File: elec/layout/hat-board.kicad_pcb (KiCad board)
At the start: 2 copper layers, 108 x 115.9 mm, 26 parts, among them U1 _NXP_Semicon_PN5321A3HN_C106_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

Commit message: 50% layout for hat
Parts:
- added C17: , lcsc:C0402, F.Cu at (104.4, 112.2)
- added C18: , lcsc:C0402, F.Cu at (109.7, 123.4)
- added C19: , lcsc:C0402, F.Cu at (179.3, 44.5)
- added C20: , lcsc:C0402, F.Cu at (188.8, 52.5)
- added C21: , lcsc:C0402, F.Cu at (196.0, 62.8)
- added C22: , lcsc:C0402, F.Cu at (164.1, 144.6)
- added C23: , lcsc:C0402, F.Cu at (139.4, 144.8)
- added C24: , lcsc:C0402, F.Cu at (117.7, 133.0)
- added C25: , lcsc:C0402, F.Cu at (101.9, 100.0)
- added C26: , lcsc:C0402, F.Cu at (101.8, 86.9)
- added C27: , lcsc:C0402, F.Cu at (201.9, 86.8)
- added C28: 100nF ±10% 16V X7R, lcsc:C0402, F.Cu at (201.8, 99.9)
- added C29: , lcsc:C0402, F.Cu at (200.4, 74.4)
- added C30: , lcsc:C0402, F.Cu at (173.9, 140.9)
- added C31: , lcsc:C0402, F.Cu at (129.5, 140.9)
- added C32: , lcsc:C0402, F.Cu at (151.7, 146.2)
- added C33: , lcsc:C0402, F.Cu at (107.6, 62.8)
- added C34: , lcsc:C0402, F.Cu at (103.2, 74.5)
- added C35: , lcsc:C0402, F.Cu at (193.8, 123.4)
- added C36: , lcsc:C0402, F.Cu at (185.8, 133.0)
- added C37: , lcsc:C0402, F.Cu at (199.3, 112.3)
- added C38: , lcsc:C0402, F.Cu at (114.8, 52.5)
- added C39: , lcsc:C0402, F.Cu at (124.3, 44.6)
- added U10: _OPSCO_Optoelectronics_SK6805SIDE_G_001, lcsc:LED-SMD_4P-L3.5-W1.6_SK6805SIDE-G-001, F.Cu at (100.6, 100.0)
- added U11: _OPSCO_Optoelectronics_SK6805SIDE_G_001, lcsc:LED-SMD_4P-L3.5-W1.6_SK6805SIDE-G-001, F.Cu at (100.4, 86.8)
- added U12: _OPSCO_Optoelectronics_SK6805SIDE_G_001, lcsc:LED-SMD_4P-L3.5-W1.6_SK6805SIDE-G-001, F.Cu at (101.9, 74.1)
- added U13: _OPSCO_Optoelectronics_SK6805SIDE_G_001, lcsc:LED-SMD_4P-L3.5-W1.6_SK6805SIDE-G-001, F.Cu at (189.8, 51.7)
- added U14: _OPSCO_Optoelectronics_SK6805SIDE_G_001, lcsc:LED-SMD_4P-L3.5-W1.6_SK6805SIDE-G-001, F.Cu at (106.4, 62.1)
- added U15: _OPSCO_Optoelectronics_SK6805SIDE_G_001, lcsc:LED-SMD_4P-L3.5-W1.6_SK6805SIDE-G-001, F.Cu at (113.8, 51.7)
- added U16: _OPSCO_Optoelectronics_SK6805SIDE_G_001, lcsc:LED-SMD_4P-L3.5-W1.6_SK6805SIDE-G-001, F.Cu at (123.5, 43.4)
- added U17: _OPSCO_Optoelectronics_SK6805SIDE_G_001, lcsc:LED-SMD_4P-L3.5-W1.6_SK6805SIDE-G-001, F.Cu at (197.2, 62.1)
- added U18: _OPSCO_Optoelectronics_SK6805SIDE_G_001, lcsc:LED-SMD_4P-L3.5-W1.6_SK6805SIDE-G-001, F.Cu at (201.7, 74.0)
- added U19: _OPSCO_Optoelectronics_SK6805SIDE_G_001, lcsc:LED-SMD_4P-L3.5-W1.6_SK6805SIDE-G-001, F.Cu at (203.2, 86.8)
- added U2: _OPSCO_Optoelectronics_SK6805SIDE_G_001, lcsc:LED-SMD_4P-L3.5-W1.6_SK6805SIDE-G-001, F.Cu at (180.1, 43.4)
- added U20: _OPSCO_Optoelectronics_SK6805SIDE_G_001, lcsc:LED-SMD_4P-L3.5-W1.6_SK6805SIDE-G-001, F.Cu at (203.0, 100.0)
- added U21: _OPSCO_Optoelectronics_SK6805SIDE_G_001, lcsc:LED-SMD_4P-L3.5-W1.6_SK6805SIDE-G-001, F.Cu at (200.5, 112.6)
- added U22: _OPSCO_Optoelectronics_SK6805SIDE_G_001, lcsc:LED-SMD_4P-L3.5-W1.6_SK6805SIDE-G-001, F.Cu at (195.0, 124.1)
- added U23: _OPSCO_Optoelectronics_SK6805SIDE_G_001, lcsc:LED-SMD_4P-L3.5-W1.6_SK6805SIDE-G-001, F.Cu at (186.7, 133.8)
- added U24: _OPSCO_Optoelectronics_SK6805SIDE_G_001, lcsc:LED-SMD_4P-L3.5-W1.6_SK6805SIDE-G-001, F.Cu at (176.4, 141.3)
- added U3: _OPSCO_Optoelectronics_SK6805SIDE_G_001, lcsc:LED-SMD_4P-L3.5-W1.6_SK6805SIDE-G-001, F.Cu at (164.4, 145.9)
- added U4: _OPSCO_Optoelectronics_SK6805SIDE_G_001, lcsc:LED-SMD_4P-L3.5-W1.6_SK6805SIDE-G-001, F.Cu at (151.8, 147.6)
- added U5: _OPSCO_Optoelectronics_SK6805SIDE_G_001, lcsc:LED-SMD_4P-L3.5-W1.6_SK6805SIDE-G-001, F.Cu at (139.1, 146.0)
- added U6: _OPSCO_Optoelectronics_SK6805SIDE_G_001, lcsc:LED-SMD_4P-L3.5-W1.6_SK6805SIDE-G-001, F.Cu at (127.3, 141.3)
- added U7: _OPSCO_Optoelectronics_SK6805SIDE_G_001, lcsc:LED-SMD_4P-L3.5-W1.6_SK6805SIDE-G-001, F.Cu at (116.9, 133.9)
- added U8: _OPSCO_Optoelectronics_SK6805SIDE_G_001, lcsc:LED-SMD_4P-L3.5-W1.6_SK6805SIDE-G-001, F.Cu at (108.7, 124.1)
- added U9: _OPSCO_Optoelectronics_SK6805SIDE_G_001, lcsc:LED-SMD_4P-L3.5-W1.6_SK6805SIDE-G-001, F.Cu at (103.1, 112.6)
- C11: value 100nF ±10% 16V X7R -> (none)
- moved C2 255.4 mm to (-3.05, -1.80), turned to 90 degrees
- moved R3 248.3 mm to (-3.00, -3.00)
- moved XTAL1 248.3 mm to (0.00, 0.00)
- moved C1 242.0 mm to (3.05, 0.10), turned to 270 degrees
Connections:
- net board_to_board_connector-net renamed reset
- net board_to_board_connector-net-2 renamed i2c_sda
- net board_to_board_connector-net-3 renamed board_to_board_connector.board_to_board_connector-net
- net board_to_board_connector-net-4 renamed touch_irq
- net board_to_board_connector-net-6 renamed nfc_irq
- net board_to_board_connector-net-7 renamed board_to_board_connector.board_to_board_connector-net-1
- net board_to_board_connector-net-8 renamed i2c_scl
- C1 pad 2: nfc-net -> gnd
- C10 pad 1: nfc-net-1 -> power_3v3
- C10 pad 2: nfc-net -> gnd
- C11 pad 1: nfc-net -> gnd
- C12 pad 2: nfc-net-5 -> nfc-net-8
- C13 pad 2: nfc-net -> gnd
- C14 pad 2: nfc-signal -> nfc-signal-1
- C15 pad 2: nfc-net -> gnd
- C2 pad 1: nfc-net-3 -> nfc-net
- C2 pad 2: nfc-net -> gnd
- C3 pad 1: nfc-net-1 -> power_3v3
- C3 pad 2: nfc-net -> gnd
- C4 pad 1: nfc-net-1 -> power_3v3
- C4 pad 2: nfc-net -> gnd
- C5 pad 1: nfc-net-1 -> power_3v3
- C5 pad 2: nfc-net -> gnd
- C6 pad 1: nfc-net-1 -> power_3v3
- C6 pad 2: nfc-net -> gnd
- C7 pad 1: nfc-net-2 -> nfc-net-3
- C8 pad 1: nfc-net-1 -> power_3v3
- C8 pad 2: nfc-net -> gnd
- C9 pad 1: nfc-net-1 -> power_3v3
- C9 pad 2: nfc-net -> gnd
- FPC1 pad 10: board_to_board_connector-net-5 -> led_data
- FPC1 pad 3: board_to_board_connector-net-9 -> lv
- FPC1 pad 4: board_to_board_connector-net-10 -> power_5v
- FPC1 pad 5: board_to_board_connector-net-11 -> power_3v3
- FPC1 pad 6: board_to_board_connector-net-1 -> gnd
- L1 pad 2: nfc-net-9 -> nfc-net-4
- L2 pad 2: nfc-net-10 -> nfc-net-7
- R1 pad 1: nfc-net-4 -> nfc-net-6
- R2 pad 1: nfc-net-8 -> nfc-net-1
- R3 pad 2: nfc-net-7 -> nfc-net-5
- R4 pad 1: nfc-net-5 -> nfc-net-8
- R4 pad 2: nfc-net-6 -> nfc-net-2
- R5 pad 1: nfc-net -> gnd
- R5 pad 2: nfc-net-6 -> nfc-net-2
- U1 pad 1: nfc-net -> gnd
- U1 pad 10: nfc-net-6 -> nfc-net-2
- U1 pad 11: nfc-net -> gnd
- U1 pad 14: nfc-net-3 -> nfc-net
- U1 pad 15: nfc-net-7 -> nfc-net-5
- U1 pad 16: nfc-net-1 -> power_3v3
- U1 pad 17: nfc-net -> gnd
- U1 pad 18: nfc-net -> gnd
- U1 pad 23: nfc-net-1 -> power_3v3
- U1 pad 25: nfc-signal-1 -> p70_irq
- U1 pad 26: rstout_n -> nfc-signal
- U1 pad 27: nfc-net-8 -> nfc-net-1
- U1 pad 28: nfc-net-4 -> nfc-net-6
- U1 pad 3: nfc-net -> gnd
- U1 pad 37: nfc-net-2 -> nfc-net-3
- U1 pad 39: nfc-net-1 -> power_3v3
- U1 pad 4: nfc-net-9 -> nfc-net-4
- U1 pad 40: nfc-net-1 -> power_3v3
- U1 pad 41: nfc-net -> gnd
- U1 pad 5: nfc-net-1 -> power_3v3
- U1 pad 6: nfc-net-10 -> nfc-net-7
- U1 pad 7: nfc-net -> gnd
- U1 pad 8: nfc-net-1 -> power_3v3
- U1 pad 9: nfc-net -> gnd
- XTAL1 pad 1: nfc-net -> gnd
- XTAL1 pad 2: nfc-net-3 -> nfc.oscillator.crystal.footprint.pins[1].net-net
- XTAL1 pad 3: nfc.oscillator.crystal.footprint.pins[2].net-net -> nfc.oscillator-net
- XTAL1 pad 4: nfc.oscillator-net -> nfc-net
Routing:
- net lv: track 0.00 -> 103.6 mm, vias 0 -> 24
- net hv: track 0.00 -> 77.7 mm, vias 0 -> 19
- net signal-7: track 0.00 -> 26.0 mm
- net signal-21: track 0.00 -> 10.4 mm
- net signal-5: track 0.00 -> 10.4 mm
- net signal-19: track 0.00 -> 10.4 mm
- net signal-18: track 0.00 -> 10.3 mm
- net signal-16: track 0.00 -> 10.0 mm
- net signal-3: track 0.00 -> 9.99 mm
- net signal-13: track 0.00 -> 9.95 mm
- net signal-17: track 0.00 -> 9.95 mm
- net signal-8: track 0.00 -> 9.93 mm
- net signal-6: track 0.00 -> 9.90 mm
- net signal-12: track 0.00 -> 9.85 mm
- net signal-9: track 0.00 -> 9.76 mm
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- added copper zone on B.Cu, net hv
- added copper zone on B.Cu, net lv

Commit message: import antenna and button footprints
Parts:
- added C40: , lcsc:C0402, F.Cu at (154.4, 60.6)
- added C41: 220pF ±10% 50V X7R, lcsc:C0402, F.Cu at (152.1, 60.6)
- added P1: HatButtonAntenna, lcsc:hat-button-antenna, F.Cu at (151.8, 90.3)
- C15: value (none) -> 100pF ±5% 50V C0G
- C16: value (none) -> 20pF ±5% 50V C0G
- C25: value (none) -> 100nF ±10% 16V X7R
- C28: value 100nF ±10% 16V X7R -> (none)
- L1: value 15nH ±5% 300mA 500mΩ -> (none); footprint lcsc:L0402 -> lcsc:IND-SMD_L1.6-W0.8-1
- L2: value (none) -> 560nH ±5% 450mA 480mΩ; footprint lcsc:L0402 -> lcsc:IND-SMD_L1.6-W0.8-1
- R4: value (none) -> 1kΩ ±1% 62.5mW
- moved C11 185.6 mm to (150.4, 75.8), turned to -90 degrees
- moved C10 170.2 mm to (158.1, 67.1)
- moved R3 167.6 mm to (148.1, 69.6)
- moved C8 163.4 mm to (155.6, 65.4)
- moved C2 162.9 mm to (145.9, 64.2), turned to 0 degrees
- moved C9 162.2 mm to (155.8, 64.2)
- moved XTAL1 160.9 mm to (146.4, 66.8), turned to 90 degrees
- moved C1 158.9 mm to (146.0, 69.6), turned to 180 degrees
- moved C7 150.4 mm to (158.1, 69.0)
- moved C6 145.4 mm to (151.7, 75.0), turned to -90 degrees
- moved C4 140.7 mm to (147.7, 70.9), turned to 180 degrees
- moved C5 130.1 mm to (158.1, 68.0)
- moved C3 129.2 mm to (151.6, 65.0), turned to 90 degrees
- moved R2 104.8 mm to (153.9, 75.2), turned to -90 degrees
- moved R1 93.5 mm to (155.9, 75.2), turned to -90 degrees
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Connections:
- C13 pad 1: tx_1_mid -> nfc-net-7
- C14 pad 2: nfc-signal-1 -> nfc-net-7
- C15 pad 1: tx_2_mid -> nfc-net-1
- C16 pad 2: nfc-signal-2 -> nfc-net-1
- C2 pad 1: nfc-net -> nfc-net-4
- L1 pad 2: nfc-net-4 -> nfc-net-2
- L2 pad 2: nfc-net-7 -> nfc-net-10
- R1 pad 1: nfc-net-6 -> nfc-net
- R2 pad 1: nfc-net-1 -> nfc-net-5
- R3 pad 2: nfc-net-5 -> nfc-net-6
- R4 pad 2: nfc-net-2 -> nfc-net-9
- R5 pad 2: nfc-net-2 -> nfc-net-9
- U1 pad 10: nfc-net-2 -> nfc-net-9
- U1 pad 14: nfc-net -> nfc-net-4
- U1 pad 15: nfc-net-5 -> nfc-net-6
- U1 pad 25: p70_irq -> nfc-signal
- U1 pad 26: nfc-signal -> rstout_n
- U1 pad 27: nfc-net-1 -> nfc-net-5
- U1 pad 28: nfc-net-6 -> nfc-net
- U1 pad 4: nfc-net-4 -> nfc-net-2
- U1 pad 6: nfc-net-7 -> nfc-net-10
- U10 pad 1: signal-11 -> signal-6
- U10 pad 4: signal-12 -> signal-20
- U11 pad 1: signal-14 -> signal-5
- U11 pad 4: signal-11 -> signal-6
- U12 pad 1: signal-13 -> signal-17
- U12 pad 4: signal-14 -> signal-5
- U13 pad 1: signal-19 -> signal-7
- U13 pad 4: signal-10 -> signal-8
- U14 pad 1: signal-20 -> signal-14
- U14 pad 4: signal-13 -> signal-17
- U15 pad 1: signal-15 -> signal-2
- U15 pad 4: signal-20 -> signal-14
- U16 pad 4: signal-15 -> signal-2
- U17 pad 1: signal-21 -> signal-16
- U17 pad 4: signal-19 -> signal-7
- U18 pad 1: signal-7 -> signal-15
- U18 pad 4: signal-21 -> signal-16
- U19 pad 1: signal-6 -> signal-19
- U19 pad 4: signal-7 -> signal-15
- U2 pad 1: signal-10 -> signal-8
- U20 pad 1: signal-5 -> signal-18
- U20 pad 4: signal-6 -> signal-19
- U21 pad 1: signal-4 -> signal-21
- U21 pad 4: signal-5 -> signal-18
- U22 pad 1: signal-18 -> signal-11
- U22 pad 4: signal-4 -> signal-21
- U23 pad 1: signal-3 -> signal-10
- U23 pad 4: signal-18 -> signal-11
- U24 pad 4: signal-3 -> signal-10
- U4 pad 1: signal-2 -> signal-9
- U5 pad 1: signal-17 -> signal-13
- U5 pad 4: signal-2 -> signal-9
- U6 pad 1: signal-16 -> signal-12
- U6 pad 4: signal-17 -> signal-13
- U7 pad 1: signal-9 -> signal-4
- U7 pad 4: signal-16 -> signal-12
- U8 pad 1: signal-8 -> signal-3
- U8 pad 4: signal-9 -> signal-4
- U9 pad 1: signal-12 -> signal-20
- U9 pad 4: signal-8 -> signal-3
- XTAL1 pad 1: gnd -> nfc.oscillator-net
- XTAL1 pad 2: nfc.oscillator.crystal.footprint.pins[1].net-net -> gnd
- XTAL1 pad 3: nfc.oscillator-net -> nfc-net-4
- XTAL1 pad 4: nfc-net -> gnd
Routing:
- net power_5v: track 0.00 -> 77.7 mm, vias 0 -> 19
- net hv: track 77.7 -> 0.00 mm, vias 19 -> 0
- net gnd: track 0.00 -> 29.9 mm, vias 0 -> 1
- net led_data: track 0.00 -> 26.0 mm
- net signal-7: track 26.0 -> 9.99 mm
- net power_3v3: track 0.00 -> 12.3 mm, vias 0 -> 3
- net (no net): track 9.72 -> 0.00 mm
- net nfc-net-4: track 0.00 -> 8.31 mm
- net nfc-net-2: track 0.00 -> 3.96 mm
- net nfc-net-10: track 0.00 -> 3.91 mm
- net tx_2_mid: track 0.00 -> 3.78 mm
- net nfc-net-5: track 0.00 -> 3.66 mm
- net nfc-net-9: track 0.00 -> 2.75 mm
- net nfc-net: track 1.99 -> 4.67 mm
- net tx_1_mid: track 0.00 -> 2.42 mm
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- added copper zone on B.Cu, net power_5v
- removed copper zone on B.Cu, net hv

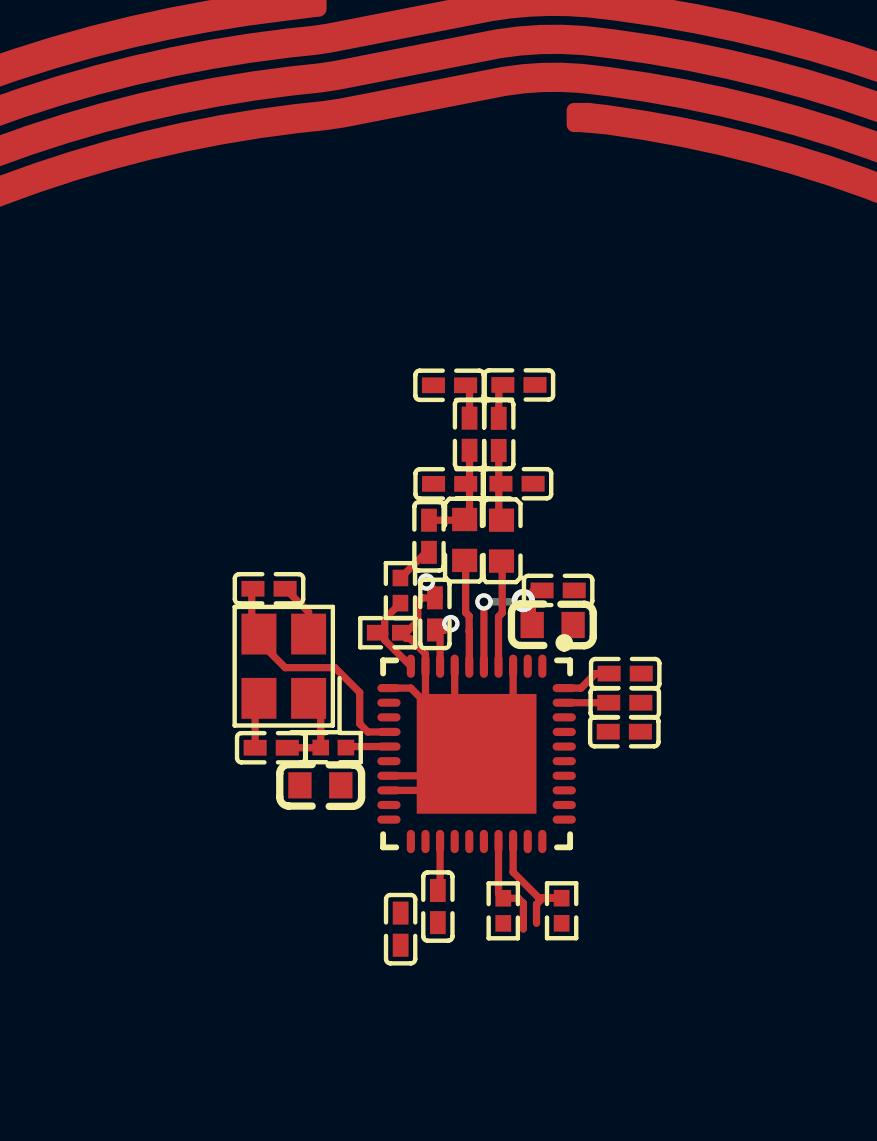
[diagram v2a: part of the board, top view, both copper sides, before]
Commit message: add capacitive sensor IC and cleanup
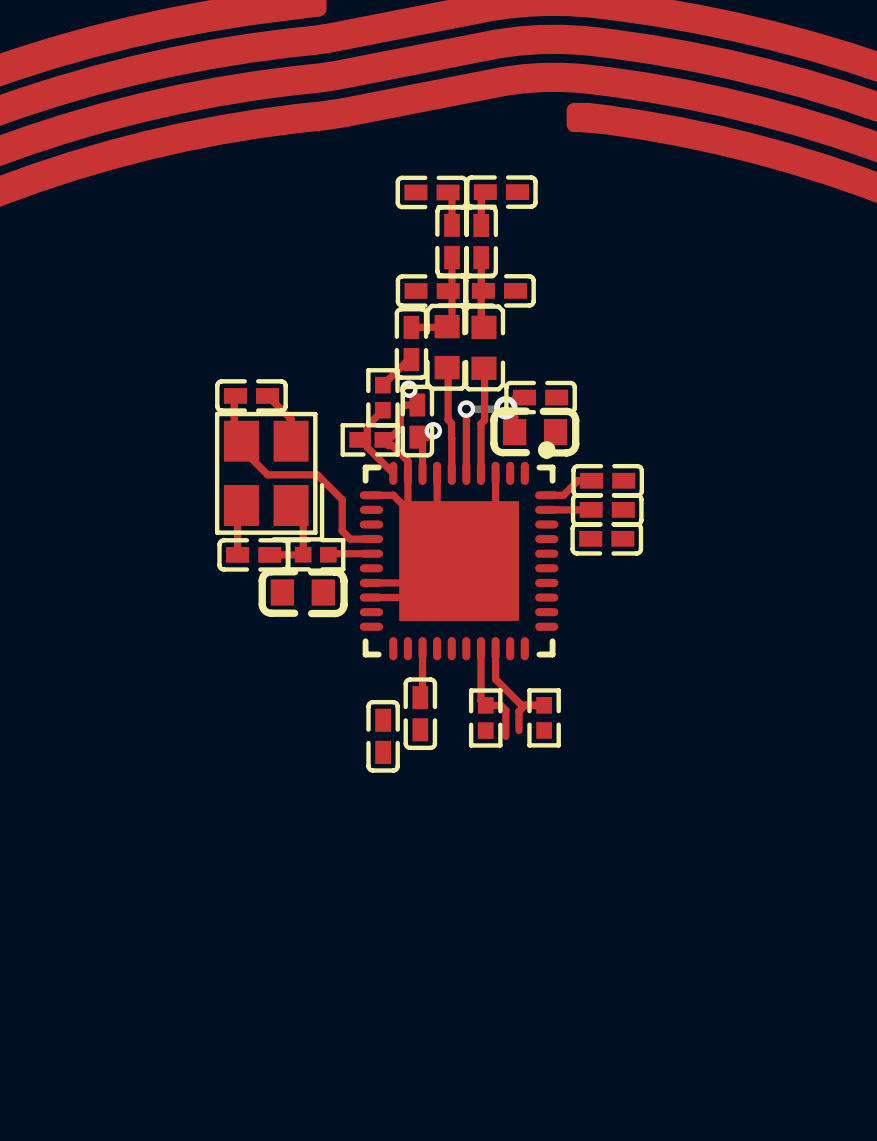
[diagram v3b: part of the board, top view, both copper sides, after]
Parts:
- moved C2 6.63 mm to (145.3, 57.5)
- moved R2 6.63 mm to (153.3, 68.6)
- moved C4 6.63 mm to (147.1, 64.3)
- moved C13 6.63 mm to (153.8, 50.6)
- moved C41 6.63 mm to (151.5, 54.0)
- moved C8 6.63 mm to (155.0, 58.8)
- moved C9 6.63 mm to (155.2, 57.6)
- moved C1 6.63 mm to (145.4, 63.0)
- moved C12 6.63 mm to (150.8, 55.8)
- moved C14 6.63 mm to (153.2, 52.3)
- moved C15 6.63 mm to (151.5, 50.6)
- moved C16 6.63 mm to (152.2, 52.3)
- moved C40 6.63 mm to (153.8, 54.0)
- moved L2 6.63 mm to (152.0, 55.9)
- moved R3 6.63 mm to (147.5, 63.0)
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
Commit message: builds working
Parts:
- added C42: 100nF ±10% 16V X7R, lcsc:C0402, F.Cu at (158.0, 76.2)
- added R10: 10kΩ ±1% 62.5mW, lcsc:R0402, F.Cu at (157.8, 75.1)
- added R6: 10kΩ ±1% 62.5mW, lcsc:R0402, F.Cu at (158.6, 111.0)
- added R7: 5.1kΩ ±1% 62.5mW, lcsc:R0402, F.Cu at (152.9, 73.2)
- added R8: 5.1kΩ ±1% 62.5mW, lcsc:R0402, F.Cu at (153.9, 73.2)
- added R9: 10kΩ ±1% 62.5mW, lcsc:R0402, F.Cu at (152.1, 80.7)
- added U25: _Microchip_Tech_CAP1188_1_CP_TR, lcsc:QFN-24_L4.0-W4.0-P0.50-TL-EP2.5, F.Cu at (153.6, 77.0)
- C1, C14, C2: value (none) -> 20pF ±5% 50V C0G
- C10, C11, C12, C17, C18, C19, C20, C21, C22, C23, C24, C26, C27, C28, C29, C3, C30, C31, C32, C33, C34, C35, C36, C37, C38, C39, C5, C6, C7, C9: value (none) -> 100nF ±10% 16V X7R
- C13: value (none) -> 100pF ±5% 50V C0G
- C40: value (none) -> 220pF ±10% 50V X7R
- C8: value (none) -> 10µF ±10% 10V X5R
- L1: value (none) -> 560nH ±5% 450mA 480mΩ
- R1: value 10Ω ±1% 62.5mW -> 5.1kΩ ±1% 62.5mW
- R2, R3, R5: value (none) -> 5.1kΩ ±1% 62.5mW
- moved R3 14.7 mm to (132.8, 62.2)
- moved C1 12.8 mm to (132.8, 65.1), turned to 90 degrees
- moved XTAL1 11.2 mm to (135.8, 65.2), turned to 0 degrees
- moved C2 10.1 mm to (138.8, 65.3), turned to -90 degrees
- moved P1 0.80 mm to (151.8, 91.1)
- moved FPC1 0.20 mm to (151.8, 36.2)
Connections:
- C12 pad 2: nfc-net-8 -> nfc-net
- C13 pad 1: nfc-net-7 -> antenna_p
- C14 pad 2: nfc-net-7 -> antenna_p
- C15 pad 1: nfc-net-1 -> antenna_n
- C16 pad 2: nfc-net-1 -> antenna_n
- C2 pad 1: nfc-net-4 -> nfc-net-5
- C7 pad 1: nfc-net-3 -> nfc-net-4
- L1 pad 2: nfc-net-2 -> nfc-net-1
- L2 pad 2: nfc-net-10 -> nfc-net-6
- P1 pad 1: hat_button_antenna.footprint.pins[0].net-net -> prev_button
- P1 pad 10: hat_button_antenna.footprint.pins[1].net-net -> antenna_p
- P1 pad 2: hat_button_antenna.footprint.pins[2].net-net -> play_button
- P1 pad 3: hat_button_antenna.footprint.pins[3].net-net -> next_button
- P1 pad 4: hat_button_antenna.footprint.pins[4].net-net -> slider_0
- P1 pad 5: hat_button_antenna.footprint.pins[5].net-net -> slider_1
- P1 pad 6: hat_button_antenna.footprint.pins[6].net-net -> slider_2
- P1 pad 7: hat_button_antenna.footprint.pins[7].net-net -> slider_3
- P1 pad 8: hat_button_antenna.footprint.pins[8].net-net -> slider_4
- P1 pad 9: hat_button_antenna.footprint.pins[9].net-net -> antenna_n
- R1 pad 1: nfc-net -> i2c_scl
- R2 pad 1: nfc-net-5 -> i2c_sda
- R3 pad 2: nfc-net-6 -> nfc-net-3
- R4 pad 1: nfc-net-8 -> nfc-net
- R4 pad 2: nfc-net-9 -> nfc-net-2
- R5 pad 2: nfc-net-9 -> nfc-net-2
- U1 pad 10: nfc-net-9 -> nfc-net-2
- U1 pad 14: nfc-net-4 -> nfc-net-5
- U1 pad 15: nfc-net-6 -> nfc-net-3
- U1 pad 25: nfc-signal -> nfc_irq
- U1 pad 26: rstout_n -> reset
- U1 pad 27: nfc-net-5 -> i2c_sda
- U1 pad 28: nfc-net -> i2c_scl
- U1 pad 37: nfc-net-3 -> nfc-net-4
- U1 pad 4: nfc-net-2 -> nfc-net-1
- U1 pad 6: nfc-net-10 -> nfc-net-6
- U10 pad 1: signal-6 -> signal-10
- U10 pad 4: signal-20 -> signal-2
- U11 pad 1: signal-5 -> signal-16
- U11 pad 4: signal-6 -> signal-10
- U12 pad 1: signal-17 -> signal-15
- U12 pad 4: signal-5 -> signal-16
- U13 pad 1: signal-7 -> signal-13
- U13 pad 4: signal-8 -> signal-14
- U14 pad 1: signal-14 -> signal-21
- U14 pad 4: signal-17 -> signal-15
- U15 pad 1: signal-2 -> signal-5
- U15 pad 4: signal-14 -> signal-21
- U16 pad 4: signal-2 -> signal-5
- U17 pad 1: signal-16 -> signal-17
- U17 pad 4: signal-7 -> signal-13
- U18 pad 1: signal-15 -> signal-9
- U18 pad 4: signal-16 -> signal-17
- U19 pad 1: signal-19 -> signal-8
- U19 pad 4: signal-15 -> signal-9
- U2 pad 1: signal-8 -> signal-14
- U20 pad 1: signal-18 -> signal-7
- U20 pad 4: signal-19 -> signal-8
- U21 pad 1: signal-21 -> signal-6
- U21 pad 4: signal-18 -> signal-7
- U22 pad 1: signal-11 -> signal-20
- U22 pad 4: signal-21 -> signal-6
- U23 pad 1: signal-10 -> signal-1
- U23 pad 4: signal-11 -> signal-20
- U24 pad 1: signal-1 -> signal
- U24 pad 4: signal-10 -> signal-1
- U3 pad 1: signal -> signal-4
- U3 pad 4: signal-1 -> signal
- U4 pad 1: signal-9 -> signal-18
- U4 pad 4: signal -> signal-4
- U5 pad 1: signal-13 -> signal-19
- U5 pad 4: signal-9 -> signal-18
- U6 pad 4: signal-13 -> signal-19
- U7 pad 1: signal-4 -> signal-11
- U8 pad 4: signal-4 -> signal-11
- U9 pad 1: signal-20 -> signal-2
- XTAL1 pad 3: nfc-net-4 -> nfc-net-5
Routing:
- net nfc-net-4: track 8.31 -> 0.00 mm
- net i2c_scl: track 0.00 -> 4.67 mm
- net nfc-net-5: track 3.66 -> 8.31 mm
- net nfc-net-10: track 3.91 -> 0.00 mm
- net i2c_sda: track 0.00 -> 3.66 mm
- net nfc-net: track 4.67 -> 1.57 mm
- net nfc-net-1: track 1.18 -> 3.96 mm
- net nfc-net-9: track 2.75 -> 0.00 mm
- net nfc-net-6: track 1.49 -> 3.91 mm
- net capacitive_sensor-net-2: track 0.00 -> 2.08 mm
- net capacitive_sensor-net-4: track 0.00 -> 1.88 mm
- net slider_4: track 0.00 -> 1.66 mm, vias 0 -> 1
- net capacitive_sensor-net: track 0.00 -> 1.58 mm
- net nfc-net-8: track 1.57 -> 0.00 mm
- net nfc-net-3: track 0.00 -> 1.49 mm
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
